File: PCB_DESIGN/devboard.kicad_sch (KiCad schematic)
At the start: 21 parts, among them J1 USB_C_Receptacle_USB2.0_14P, U1 RP2040, U2 NCP1117-3.3_SOT223

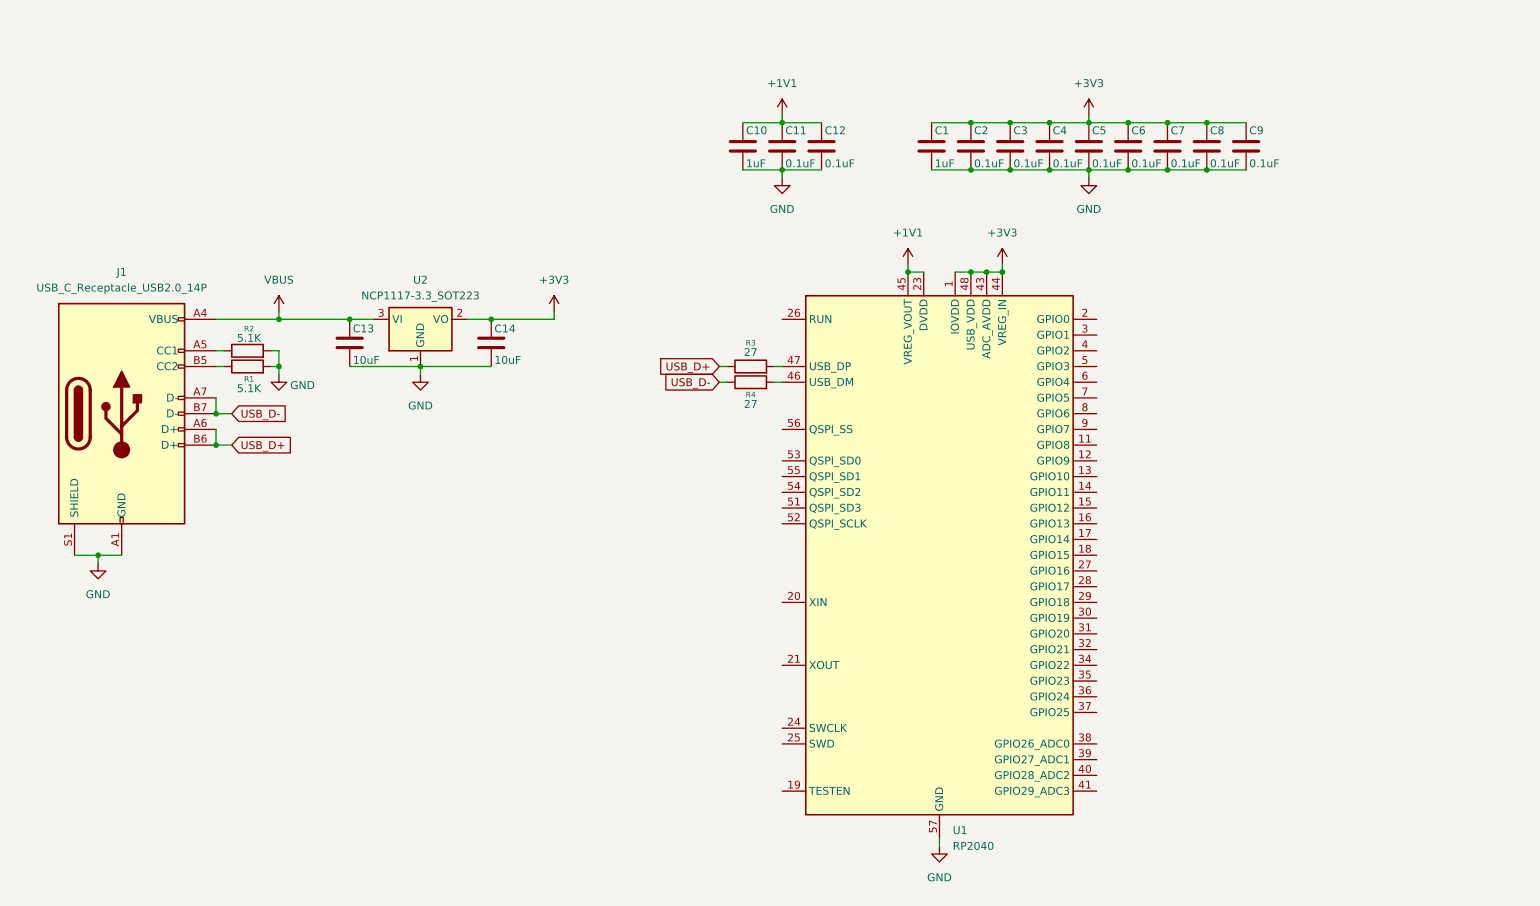
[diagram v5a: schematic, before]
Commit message: added crystal
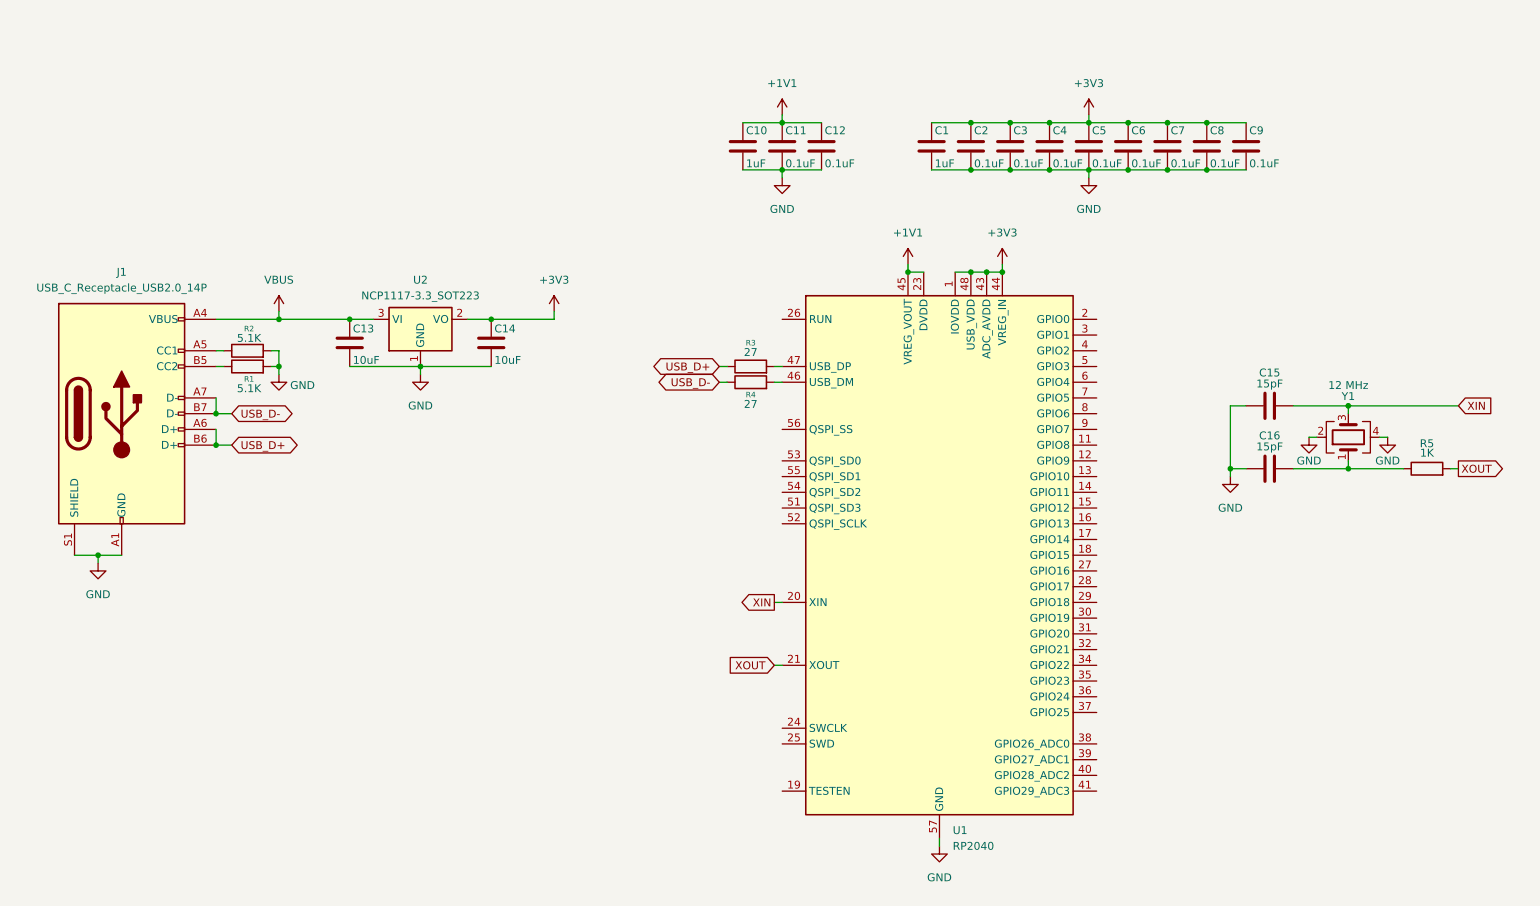
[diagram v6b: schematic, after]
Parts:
- added C15, C16: 15pF, symbol Device:C
- added R5: 1K, symbol Device:R
- added Y1: 12 MHz, symbol Device:Crystal_GND24
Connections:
- net GND: now also C15.1, C16.1, Y1.2, Y1.4
- net XIN: now reaches U1.20 (XIN)
- net XIN: now also C15.2, Y1.3
- net XOUT: now reaches U1.21 (XOUT)
- net XOUT: now also R5.2
- new net: C16.2, R5.1, Y1.1

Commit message: added flash memory
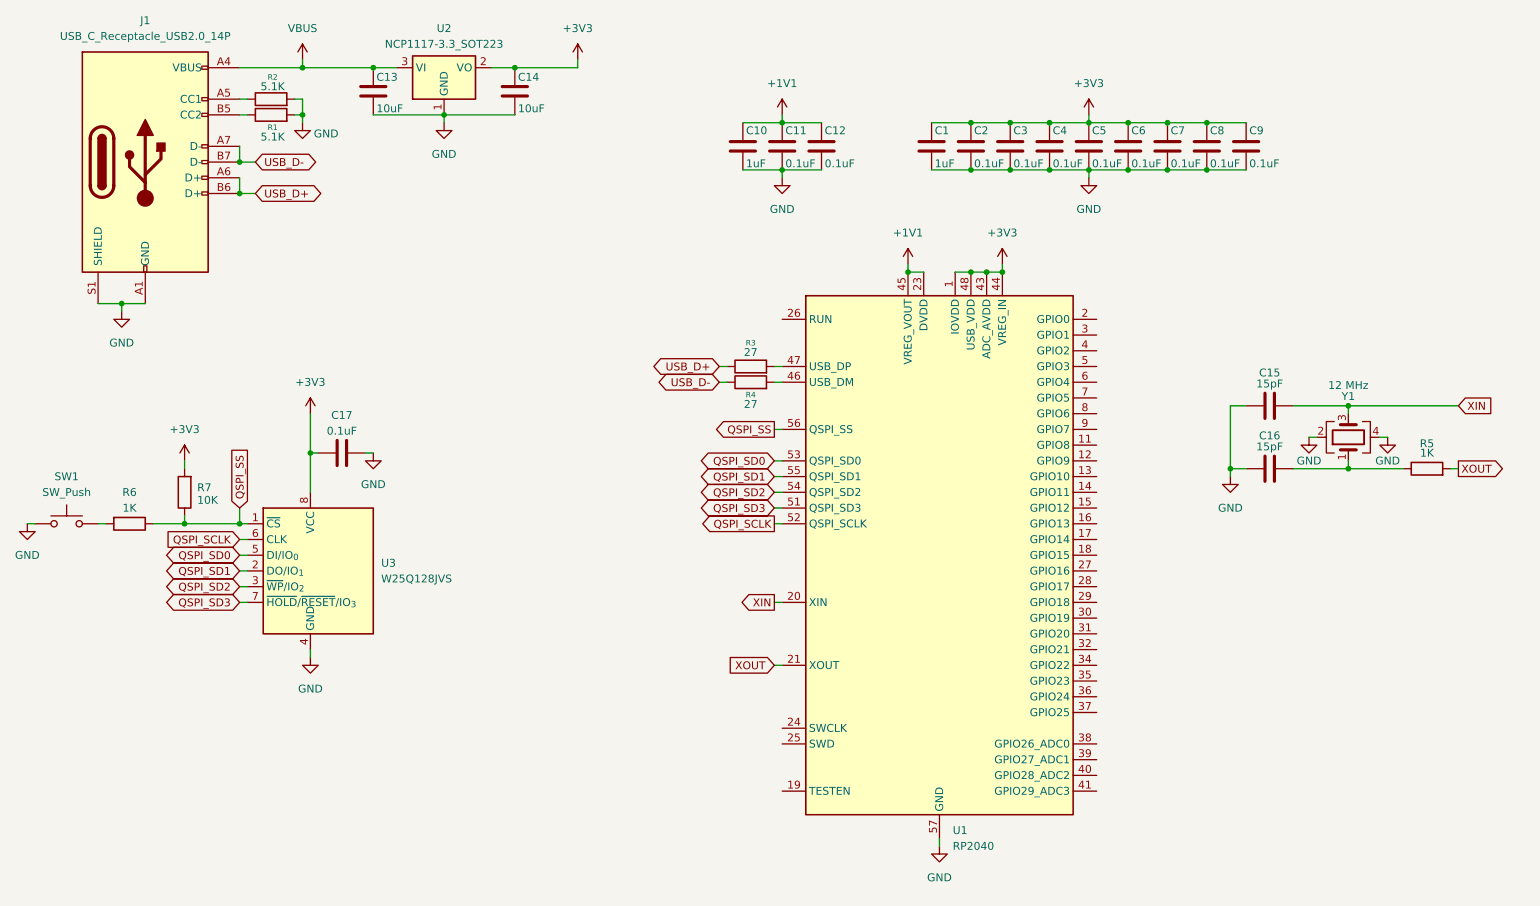
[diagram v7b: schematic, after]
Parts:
- added C17: 0.1uF, symbol Device:C
- added R6: 1K, symbol Device:R
- added R7: 10K, symbol Device:R
- added SW1: SW_Push, symbol Switch:SW_Push
- added U3: W25Q128JVS, Package_SO:SOIC-8_5.3x5.3mm_P1.27mm, symbol Memory_Flash:W25Q128JVS
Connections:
- net +3V3: now also C17.1, R7.2, U3.8 (VCC)
- net GND: now also C17.2, SW1.1, U3.4 (GND)
- net QSPI_SD3: now reaches U1.51 (QSPI_SD3)
- net QSPI_SD3: now also U3.7 (~{HOLD}/~{RESET}/IO_{3})
- net QSPI_SCLK: now reaches U1.52 (QSPI_SCLK)
- net QSPI_SCLK: now also U3.6 (CLK)
- net QSPI_SD0: now reaches U1.53 (QSPI_SD0)
- net QSPI_SD0: now also U3.5 (DI/IO_{0})
- net QSPI_SD2: now reaches U1.54 (QSPI_SD2)
- net QSPI_SD2: now also U3.3 (~{WP}/IO_{2})
- net QSPI_SD1: now reaches U1.55 (QSPI_SD1)
- net QSPI_SD1: now also U3.2 (DO/IO_{1})
- net QSPI_SS: now reaches U1.56 (QSPI_SS)
- net QSPI_SS: now also R6.1, R7.1, U3.1 (~{CS})
- new net: R6.2, SW1.2
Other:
- moved on the sheet: C13, C14, J1, R1, R2, U2

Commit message: working on breakout out GPIO's
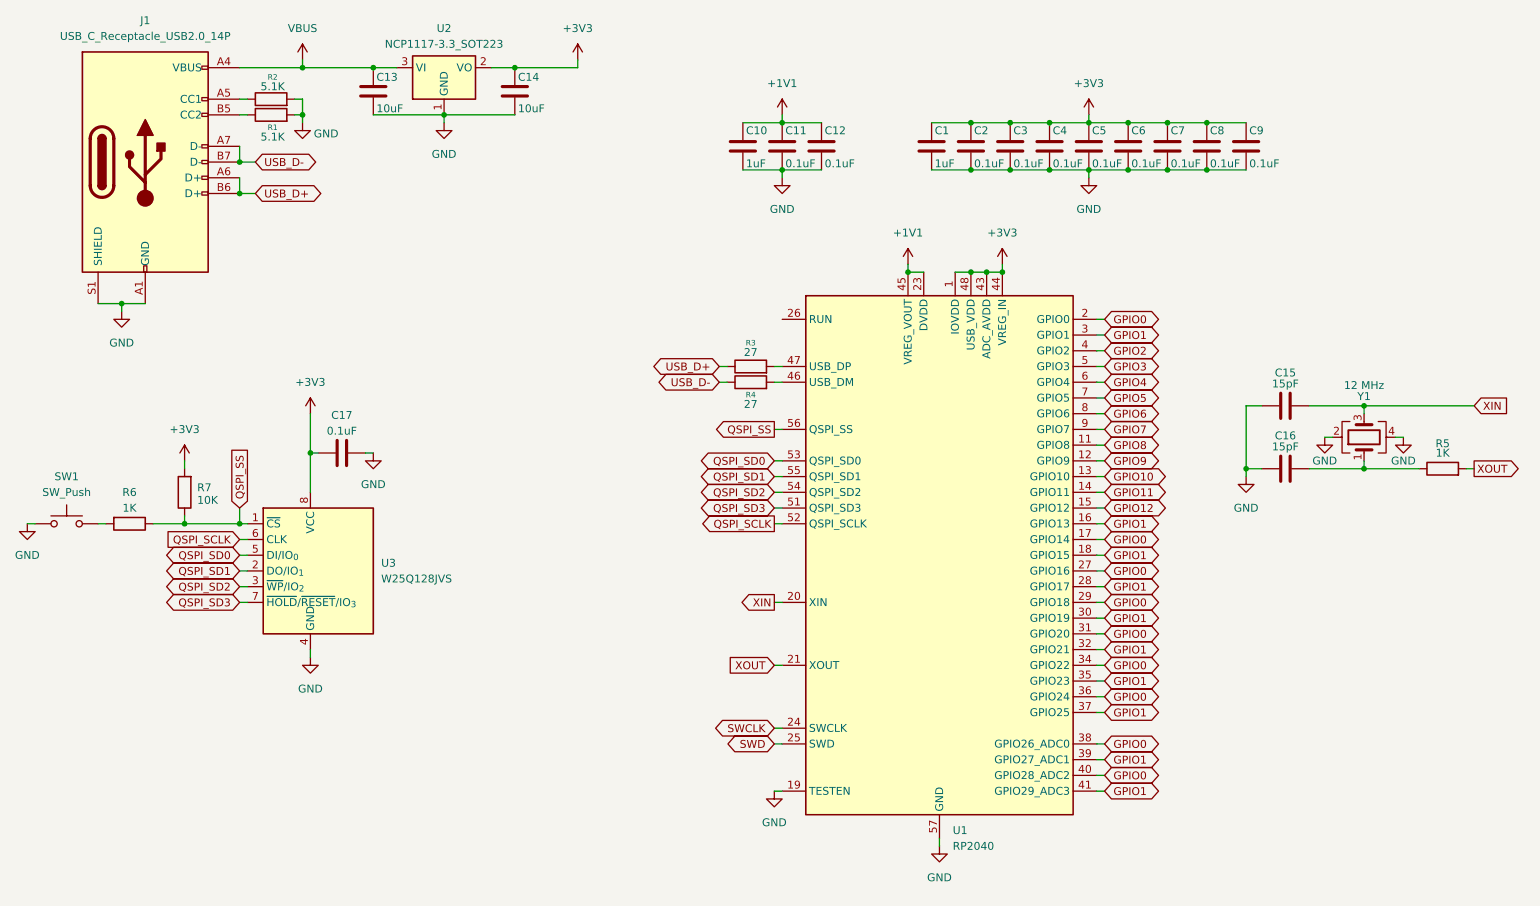
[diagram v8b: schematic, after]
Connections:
- net GND: now also U1.19 (TESTEN)
- net GPIO8: now reaches U1.11 (GPIO8)
- net GPIO9: now reaches U1.12 (GPIO9)
- net GPIO10: now reaches U1.13 (GPIO10)
- net GPIO11: now reaches U1.14 (GPIO11)
- net GPIO12: now reaches U1.15 (GPIO12)
- net GPIO1: now reaches U1.16 (GPIO13)
- net GPIO1: now also U1.18 (GPIO15), U1.28 (GPIO17), U1.3 (GPIO1), U1.30 (GPIO19), U1.32 (GPIO21), U1.35 (GPIO23), U1.37 (GPIO25), U1.39 (GPIO27_ADC1), U1.41 (GPIO29_ADC3)
- net GPIO0: now reaches U1.17 (GPIO14)
- net GPIO0: now also U1.2 (GPIO0), U1.27 (GPIO16), U1.29 (GPIO18), U1.31 (GPIO20), U1.34 (GPIO22), U1.36 (GPIO24), U1.38 (GPIO26_ADC0), U1.40 (GPIO28_ADC2)
- net SWCLK: now reaches U1.24 (SWCLK)
- net SWD: now reaches U1.25 (SWD)
- net GPIO2: now reaches U1.4 (GPIO2)
- net GPIO3: now reaches U1.5 (GPIO3)
- net GPIO4: now reaches U1.6 (GPIO4)
- net GPIO5: now reaches U1.7 (GPIO5)
- net GPIO6: now reaches U1.8 (GPIO6)
- net GPIO7: now reaches U1.9 (GPIO7)
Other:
- moved on the sheet: C15, C16, R5, Y1
